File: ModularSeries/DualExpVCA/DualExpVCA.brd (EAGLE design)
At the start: 47 x 95 mm, 71 parts, among them IC1 LM13700_DIP, IC2 TL0X4_DIP, IC3 TL0X4_DIP, Q1 2N3906, Q2 2N3906, Q3 2N3906, Q4 2N3906

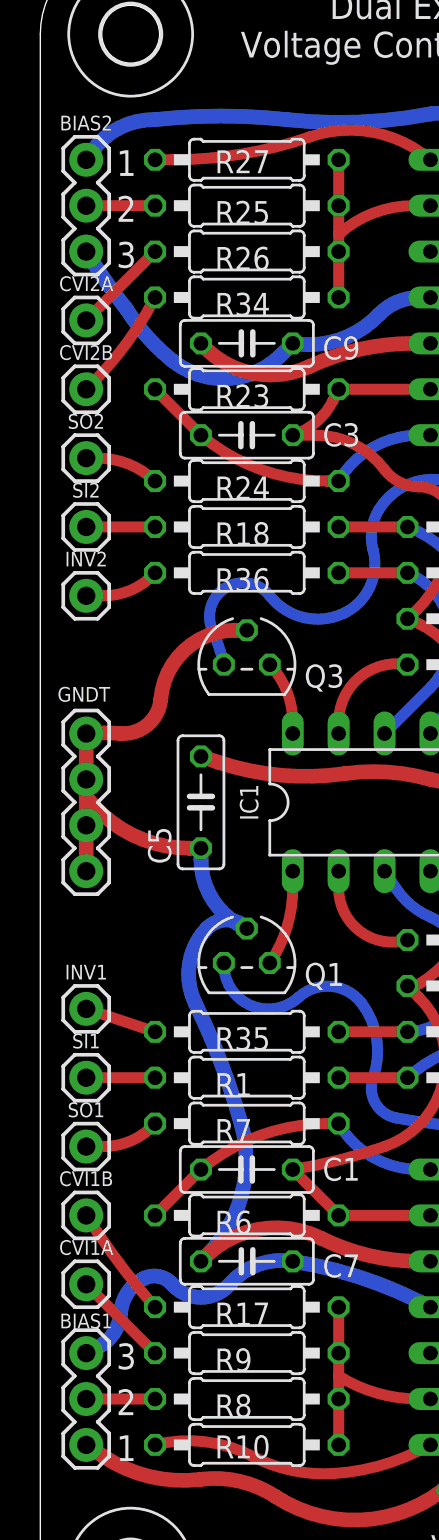
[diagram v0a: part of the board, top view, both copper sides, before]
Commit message: Updates to Prism, VCA, PSU and Prism BOM added
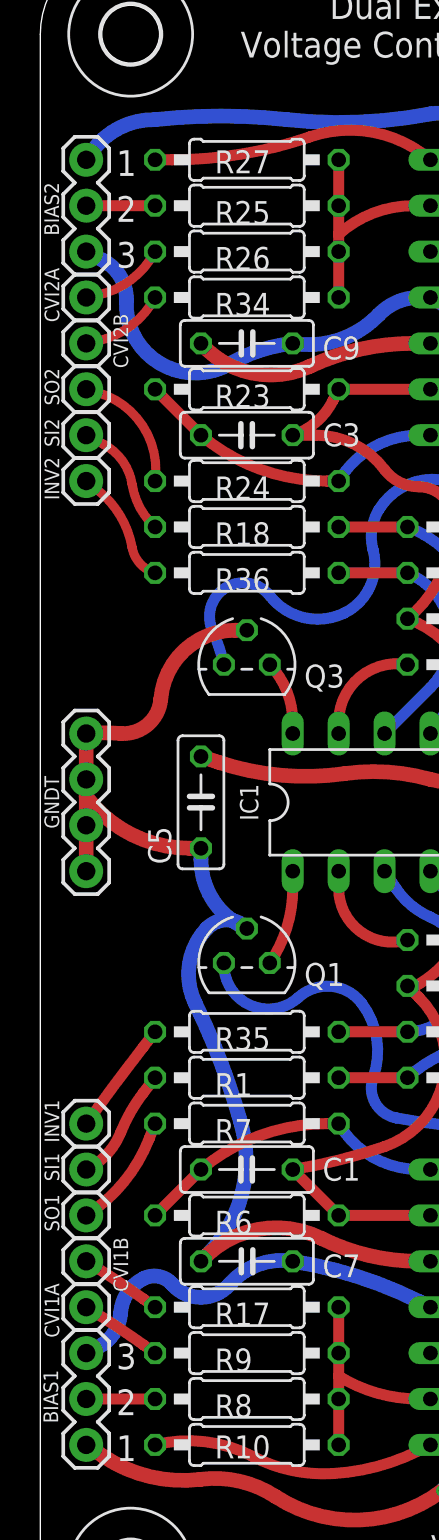
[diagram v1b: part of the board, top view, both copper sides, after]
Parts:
- moved INV1 6.35 mm to (2.54, 29.7)
- moved INV2 6.35 mm to (2.54, 65.3)
- moved SI2 5.08 mm to (2.54, 67.8)
- moved SI1 5.08 mm to (2.54, 27.2)
- moved SO1 3.81 mm to (2.54, 24.6)
- moved SO2 3.81 mm to (2.54, 70.3)
- moved CVI2B 2.54 mm to (2.54, 72.9)
- moved CVI1B 2.54 mm to (2.54, 22.1)
- moved CVI2A 1.27 mm to (2.54, 75.4)
- moved CVI1A 1.27 mm to (2.54, 19.6)
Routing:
- net N$21: track 3.81 -> 6.48 mm
- net N$1: track 3.81 -> 6.39 mm
- net N$27: track 4.05 -> 6.50 mm
- net N$41: track 4.02 -> 6.35 mm
- net N$42: track 4.08 -> 6.40 mm
- net N$6: track 4.08 -> 6.39 mm
- net N$19: track 6.35 -> 4.58 mm
- net N$40: track 6.35 -> 4.63 mm
- net N$9: track 5.39 -> 4.58 mm
- net N$29: track 5.39 -> 4.63 mm
- net +12V: track 148.1 -> 147.5 mm
